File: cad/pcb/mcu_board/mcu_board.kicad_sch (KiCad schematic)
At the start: 27 parts, among them J1 Pin header, J2 EMI Shield, J3 FFC8, J4 Display interface, Q1 BC847C, U1 MCP6001T-I/OT, U2 STM32F103CBTx, U3 NCP1117-3.3_SOT223, Y1 XC32M4-8.000 12pF

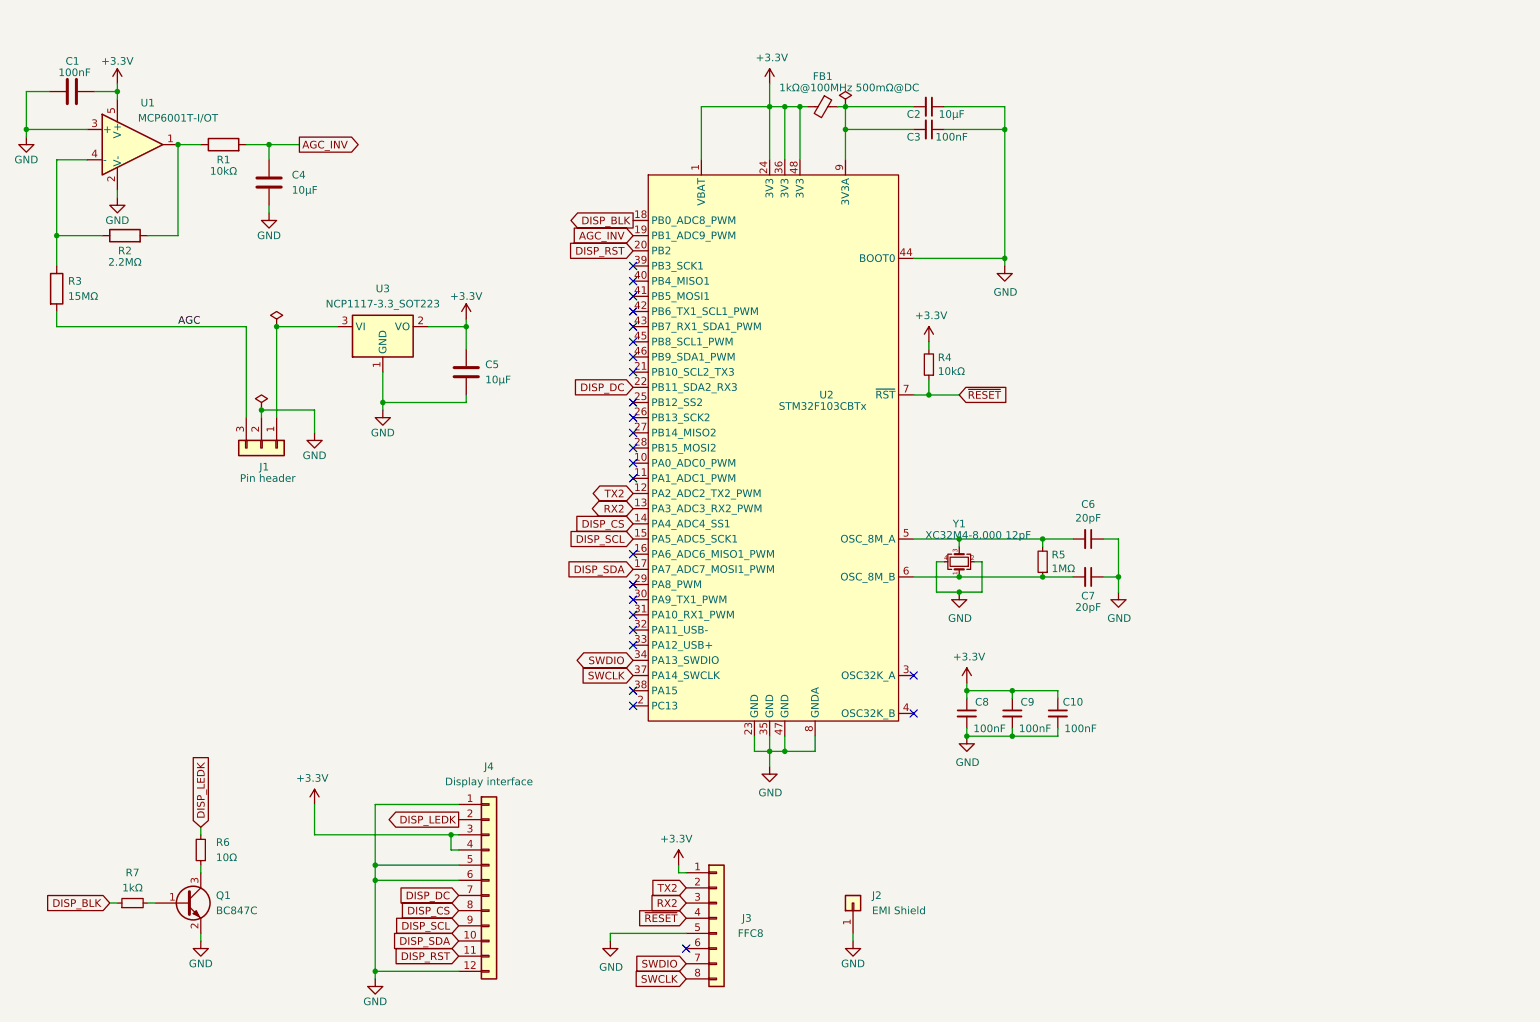
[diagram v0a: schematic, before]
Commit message: Change: Schematic 6U5 -> EM34
- use generic 1117
- add software selection straps
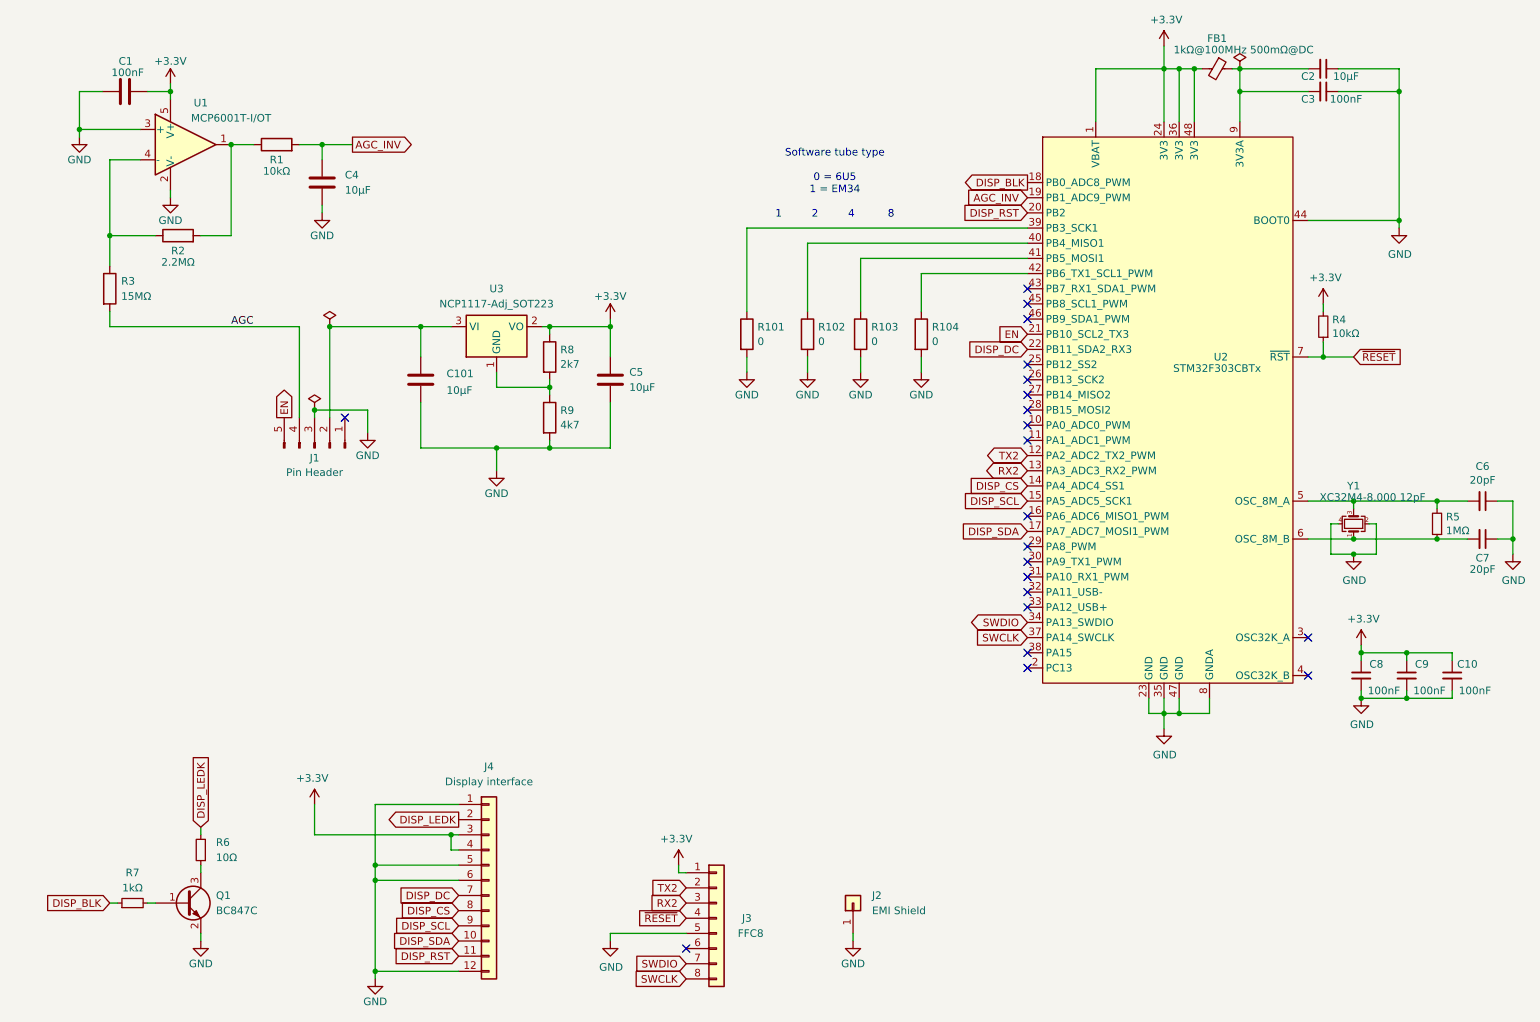
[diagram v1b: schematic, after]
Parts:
- removed J1: Pin header, Retronics_Connectors:PinHeader_1x03_P2.54mm_Horizontal_Alt, symbol Connector_Generic:Conn_01x03
- added C101: 10µF, Capacitor_SMD:C_1206_3216Metric_Pad1.33x1.80mm_HandSolder, symbol Device:C
- added J1: Pin Header, Connector_PinHeader_2.54mm:PinHeader_1x05_P2.54mm_Horizontal, symbol Connector:Conn_01x05_Pin
- added R101, R102, R103, R104: 0, Resistor_SMD:R_0603_1608Metric_Pad0.98x0.95mm_HandSolder, symbol Device:R
- added R8: 2k7, Resistor_SMD:R_0603_1608Metric_Pad0.98x0.95mm_HandSolder, symbol Device:R
- added R9: 4k7, Resistor_SMD:R_0603_1608Metric_Pad0.98x0.95mm_HandSolder, symbol Device:R
- C2: footprint Capacitor_SMD:C_0603_1608Metric_Pad1.08x0.95mm_HandSolder -> Capacitor_SMD:C_1206_3216Metric_Pad1.33x1.80mm_HandSolder
- C4, C5: footprint Retronics_Passives:C_0603_1608Metric_Pad1.08x0.95mm_HandSolder -> Capacitor_SMD:C_1206_3216Metric_Pad1.33x1.80mm_HandSolder
- U2: value STM32F103CBTx -> STM32F303CBTx
- U3: value NCP1117-3.3_SOT223 -> NCP1117-Adj_SOT223
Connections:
- net +3.3V: now also R8.1
- net AGC: now also J1.4 (Pin_4)
- net GND: now also C101.2, J1.3 (Pin_3), R101.2, R102.2, R103.2, R104.2, R9.2; no longer U3.1 (GND)
- net at U3.3 (VI): now also C101.1, J1.2 (Pin_2)
- net EN: now reaches U2.21 (PB10_SCL2_TX3)
- net EN: now also J1.5 (Pin_5)
- net at U2.39 (PB3_SCK1): now also R101.1
- net at U2.40 (PB4_MISO1): now also R102.1
- net at U2.41 (PB5_MOSI1): now also R103.1
- net at U2.42 (PB6_TX1_SCL1_PWM): now also R104.1
- new net: R8.2, R9.1, U3.1 (GND)
- no-connect marks 25 -> 21
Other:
- note added: "Software tube type 0 = 6U5 1 = EM34 1 2 4 8"
- company: Retronics - Bjørner Sandom -> Martin Wagner DL2WAG
- title: U6A MCU Board -> EM34 MCU Board
- moved on the sheet: C1, C10, C2, C3, C4, C5, C6, C7, C8, C9, FB1, R1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

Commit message: Change: Update uC PCB
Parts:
- J3: footprint myDevices:0527450897 -> Connector_PinHeader_2.54mm:PinHeader_1x08_P2.54mm_Vertical_SMD_Pin1Left
- renumbered C101 to C11, R101 to R10, R102 to R11, R103 to R12, R104 to R13
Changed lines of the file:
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@@
 		(dnp no)
 		(fields_autoplaced yes)
-		(property "Reference" "R101"
+		(property "Reference" "R10"
 			(at 140.208 76.2578 0)
 			(effects
@@
 			(project "mcu_board"
 				(path "/88323e32-4acb-49fb-898d-0e3c32abded2"
-					(reference "R101")
+					(reference "R10")
 					(unit 1)
 				)
@@
 		(on_board yes)
 		(dnp no)
-		(property "Reference" "C101"
+		(property "Reference" "C11"
 			(at 88.138 84.074 0)
 			(effects
@@
 			(project "mcu_board"
 				(path "/88323e32-4acb-49fb-898d-0e3c32abded2"
-					(reference "C101")
+					(reference "C11")
 					(unit 1)
 				)
@@
 		(dnp no)
 		(fields_autoplaced yes)
-		(property "Reference" "R102"
+		(property "Reference" "R11"
 			(at 150.368 76.2578 0)
 			(effects
@@
 			(project "mcu_board"
 				(path "/88323e32-4acb-49fb-898d-0e3c32abded2"
-					(reference "R102")
+					(reference "R11")
 					(unit 1)
 				)
@@
 			)
 		)
-		(property "Footprint" "myDevices:0527450897"
+		(property "Footprint" "Connector_PinHeader_2.54mm:PinHeader_1x08_P2.54mm_Vertical_SMD_Pin1Left"
 			(at 133.35 175.26 0)
 			(effects
@@
 		(dnp no)
 		(fields_autoplaced yes)
-		(property "Reference" "R103"
+		(property "Reference" "R12"
 			(at 159.258 76.2578 0)
 			(effects
@@
 			(project "mcu_board"
 				(path "/88323e32-4acb-49fb-898d-0e3c32abded2"
-					(reference "R103")
+					(reference "R12")
 					(unit 1)
 				)
@@
 		(dnp no)
 		(fields_autoplaced yes)
-		(property "Reference" "R104"
+		(property "Reference" "R13"
 			(at 169.418 76.2578 0)
 			(effects
@@
 			(project "mcu_board"
 				(path "/88323e32-4acb-49fb-898d-0e3c32abded2"
-					(reference "R104")
+					(reference "R13")
 					(unit 1)
 				)

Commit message: Change: Add Jtag, Cleanup
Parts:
- added J10, J3, J4, J6, J8, J9: Conn_01x01_Pin, TestPoint:TestPoint_Pad_D1.5mm, symbol Connector:Conn_01x01_Pin
- J7: renamed from J3; footprint Connector_PinHeader_2.54mm:PinHeader_1x08_P2.54mm_Vertical_SMD_Pin1Left -> Connector_PinHeader_2.54mm:PinHeader_1x08_P2.54mm_Vertical
- renumbered C2 to C1, C9 to C10, C10 to C11, C1 to C2, C11 to C5, C5 to C6, C6 to C7, C7 to C8, C8 to C9, J4 to J5, R9 to R10, R5 to R11, R6 to R12, R7 to R13, R8 to R5, R10 to R6, R11 to R7, R12 to R8, R13 to R9
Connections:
- net SWCLK: now also J4.1 (Pin_1)
- net SWDIO: now also J3.1 (Pin_1)
- net ~{RESET}: now also J10.1 (Pin_1)
- net JTDI: now reaches U2.38 (PA15)
- net JTDI: now also J6.1 (Pin_1)
- net at R6.1: now also U2.41 (PB5_MOSI1); no longer U2.39 (PB3_SCK1)
- net at R7.1: now also U2.42 (PB6_TX1_SCL1_PWM); no longer U2.40 (PB4_MISO1)
- net at R8.1: now also U2.43 (PB7_RX1_SDA1_PWM); no longer U2.41 (PB5_MOSI1)
- net at R9.1: now also U2.45 (PB8_SCL1_PWM); no longer U2.42 (PB6_TX1_SCL1_PWM)
- new net JNTRST: J9.1 (Pin_1), U2.40 (PB4_MISO1)
- new net JTDO: J8.1 (Pin_1), U2.39 (PB3_SCK1)
- no-connect marks 21 -> 19
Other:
- note added: "Debug"
- note added: "JTAG"
- moved on the sheet: J2, R6, R7, R8, R9
